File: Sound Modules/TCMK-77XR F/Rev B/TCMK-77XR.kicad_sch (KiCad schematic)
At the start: 33 parts, among them CN1 2x12 Connector Female, IC1 S-SMP, IC2 S-DSP, IC3 HM9453100FP, IC4 HM9453100FP, IC5 µPD6376, IC6 2904, X1 24.576Mhz

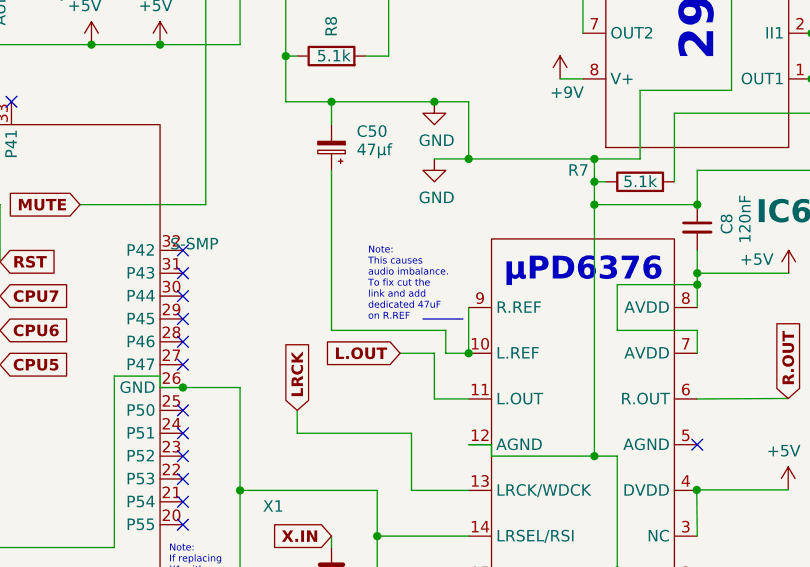
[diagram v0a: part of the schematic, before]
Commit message: Fix schema note for Audio Balance Mod
Noted the wrong pin to attach the cap to on the schematic diagram
comments.

I apologize for the mistake and thanks to /u/Yekomhxc for reporting

There was no mistake on the actual board itself.
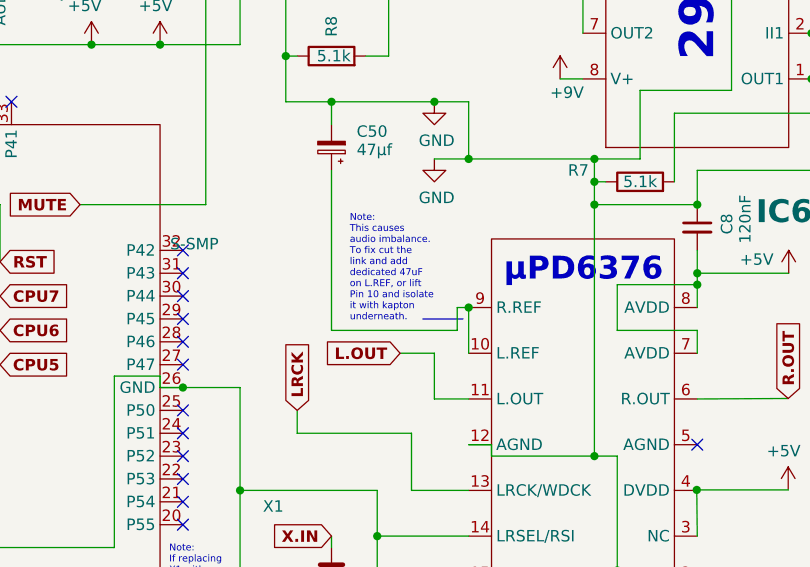
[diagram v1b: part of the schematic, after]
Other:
- note added: "Note: This causes audio imbalance. To fix cut the link and add dedicated 47uF on L.REF, or lift Pin 10 and isolate it with kapton underneath."
- note removed: "Note: This causes audio imbalance. To fix cut the link and add dedicated 47uF on R.REF"
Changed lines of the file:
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@@
 		)
 	)
-	(text "Note:\nThis causes\naudio imbalance.\nTo fix cut the \nlink and add \ndedicated 47uF\non R.REF"
+	(text "Note:\nThis causes\naudio imbalance.\nTo fix cut the \nlink and add \ndedicated 47uF\non L.REF, or lift\nPin 10 and isolate\nit with kapton\nunderneath."
 		(exclude_from_sim no)
-		(at 164.084 90.17 0)
+		(at 162.052 88.392 0)
 		(effects
 			(font
@@
 	)
 	(junction
+		(at 175.26 92.71)
+		(diameter 0)
+		(color 255 0 85 1)
+	)
+	(junction
 		(at 271.78 80.01)
 		(diameter 0)
@@
 	)
 	(junction
-		(at 175.26 97.79)
-		(diameter 0)
-		(color 180 180 180 1)
-	)
-	(junction
 		(at 130.81 22.86)
 		(diameter 0)
@@
 	(wire
 		(pts
-			(xy 172.72 97.79) (xy 175.26 97.79)
-		)
-		(stroke
-			(width 0)
-			(type default)
-			(color 180 180 180 1)
-		)
-	)
-	(wire
-		(pts
 			(xy 43.18 95.25) (xy 43.18 105.41)
 		)
@@
 	(wire
 		(pts
-			(xy 160.02 95.25) (xy 172.72 95.25)
+			(xy 160.02 95.25) (xy 173.99 95.25)
 		)
 		(stroke
 			(width 0)
 			(type default)
-			(color 180 180 180 1)
+			(color 255 0 85 1)
 		)
 	)
@@
 			(width 0)
 			(type default)
-			(color 180 180 180 1)
+			(color 255 0 85 1)
 		)
 	)
@@
 			(width 0)
 			(type default)
-			(color 255 0 85 1)
+			(color 180 180 180 1)
 		)
 	)
@@
 	(wire
 		(pts
+			(xy 173.99 95.25) (xy 173.99 92.71)
+		)
+		(stroke
+			(width 0)
+			(type default)
+			(color 255 0 85 1)
+		)
+	)
+	(wire
+		(pts
 			(xy 86.36 135.89) (xy 86.36 140.97)
 		)
@@
 	(wire
 		(pts
+			(xy 173.99 92.71) (xy 175.26 92.71)
+		)
+		(stroke
+			(width 0)
+			(type default)
+			(color 255 0 85 1)
+		)
+	)
+	(wire
+		(pts
 			(xy 210.82 176.53) (xy 242.57 176.53)
 		)
@@
 		)
 	)
-	(wire
-		(pts
-			(xy 172.72 95.25) (xy 172.72 97.79)
-		)
-		(stroke
-			(width 0)
-			(type default)
-			(color 180 180 180 1)
-		)
-	)
